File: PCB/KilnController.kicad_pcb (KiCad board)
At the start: 2 copper layers, 150 x 85 mm, 19 parts, among them J1 12V 3A PS Header, J2 Exhaust Fan Header, J3 Circulation Fan Header, J4 SD Card Module, J5 Exhaust Servo Header, J6 Intake Servo Header, Q1 FQP30N06L, Q2 FQP30N06L, U1 Raspberry Pi Pico 2W

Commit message: Current monitoring WIP
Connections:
- U1 pad 4: /SD_MISO -> /SD_SCK
- U1 pad 6: /SD_SCK -> /SD_MISO
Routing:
- net /+5V: track 147.0 -> 176.9 mm
- net /SD_SCK: track 10.2 -> 17.6 mm
- net /SD_MISO: track 10.2 -> 14.4 mm
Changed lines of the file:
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@@
 			)
 		)
-		(property "Datasheet" ""
+		(property "Datasheet" "~"
 			(at 0 0 0)
 			(layer "F.Fab")
@@
 			)
 		)
-		(property "Description" ""
+		(property "Description" "Generic screw terminal, single row, 01x04, script generated (kicad-library-utils/schlib/autogen/connector/)"
 			(at 0 0 0)
 			(layer "F.Fab")
@@
 			)
 		)
-		(property "Datasheet" ""
+		(property "Datasheet" "~"
 			(at 0 0 0)
 			(layer "F.Fab")
@@
 			)
 		)
-		(property "Description" ""
+		(property "Description" "Generic screw terminal, single row, 01x04, script generated (kicad-library-utils/schlib/autogen/connector/)"
 			(at 0 0 0)
 			(layer "F.Fab")
@@
 			)
 		)
-		(property "Datasheet" ""
+		(property "Datasheet" "~"
 			(at 0 0 0)
 			(layer "F.Fab")
@@
 			)
 		)
-		(property "Description" ""
+		(property "Description" "Generic screw terminal, single row, 01x04, script generated (kicad-library-utils/schlib/autogen/connector/)"
 			(at 0 0 0)
 			(layer "F.Fab")
@@
 			)
 		)
-		(property "Datasheet" ""
+		(property "Datasheet" "~"
 			(at 0 0 0)
 			(layer "F.Fab")
@@
 			)
 		)
-		(property "Description" ""
+		(property "Description" "Generic screw terminal, single row, 01x04, script generated (kicad-library-utils/schlib/autogen/connector/)"
 			(at 0 0 0)
 			(layer "F.Fab")
@@
 			)
 		)
-		(property "Datasheet" ""
+		(property "Datasheet" "https://datasheets.raspberrypi.com/picow/pico-2-w-datasheet.pdf"
 			(at 8.89 24.13 90)
 			(layer "F.Fab")
@@
 			(layers "*.Cu" "*.Mask")
 			(remove_unused_layers no)
-			(net 12 "/SD_MISO")
+			(net 10 "/SD_SCK")
 			(pinfunction "GP2")
 			(pintype "bidirectional")
@@
 			(layers "*.Cu" "*.Mask")
 			(remove_unused_layers no)
-			(net 10 "/SD_SCK")
+			(net 12 "/SD_MISO")
 			(pinfunction "GP4")
 			(pintype "bidirectional")
@@
 	)
 	(segment
+		(start 142 119)
+		(end 147 124)
+		(width 0.25)
+		(layer "F.Cu")
+		(net 2)
+	)
+	(segment
 		(start 89.36 88.22)
 		(end 86.82 88.22)
@@
 	)
 	(segment
-		(start 154.08 140)
-		(end 157.08 137)
+		(start 98.68 119)
+		(end 142 119)
 		(width 0.25)
 		(layer "F.Cu")
@@
 	)
 	(segment
-		(start 98.68 119)
-		(end 94.68 115)
+		(start 147 124)
+		(end 147 140)
+		(width 0.25)
+		(layer "F.Cu")
+		(net 2)
+	)
+	(segment
+		(start 154.08 140)
+		(end 157.08 137)
 		(width 0.25)
 		(layer "F.Cu")
@@
 	(segment
 		(start 145 140)
-		(end 154.08 140)
+		(end 147 140)
 		(width 0.25)
 		(layer "F.Cu")
@@
 	)
 	(segment
-		(start 131 119)
+		(start 94.68 115)
 		(end 98.68 119)
 		(width 0.25)
@@
 	)
 	(segment
-		(start 134 122)
-		(end 131 119)
-		(width 0.25)
-		(layer "F.Cu")
-		(net 2)
-	)
-	(segment
 		(start 83 111)
 		(end 83 92.04)
@@
 	)
 	(segment
+		(start 147 140)
+		(end 154.08 140)
+		(width 0.25)
+		(layer "F.Cu")
+		(net 2)
+	)
+	(segment
 		(start 94.68 115)
 		(end 90.68 111)
@@
 	)
 	(segment
-		(start 99.52 112.22)
+		(start 94.44 106)
+		(end 96.015 104.425)
+		(width 0.25)
+		(layer "F.Cu")
+		(net 10)
+	)
+	(segment
+		(start 99.825991 104.425)
+		(end 100.935 105.534009)
+		(width 0.25)
+		(layer "F.Cu")
+		(net 10)
+	)
+	(segment
+		(start 96.015 104.425)
+		(end 99.825991 104.425)
+		(width 0.25)
+		(layer "F.Cu")
+		(net 10)
+	)
+	(segment
+		(start 100.935 113.635)
 		(end 102.3 115)
 		(width 0.25)
@@
 	)
 	(segment
-		(start 99.52 106)
-		(end 99.52 112.22)
+		(start 100.935 105.534009)
+		(end 100.935 113.635)
 		(width 0.25)
 		(layer "F.Cu")
@@
 	)
 	(segment
-		(start 94.44 106)
-		(end 94.44 112.22)
+		(start 99.52 106)
+		(end 98.395 104.875)
+		(width 0.25)
+		(layer "F.Cu")
+		(net 12)
+	)
+	(segment
+		(start 95.855 105.534009)
+		(end 95.855 113.635)
 		(width 0.25)
 		(layer "F.Cu")
@@
 	)
 	(segment
-		(start 94.44 112.22)
+		(start 95.855 113.635)
 		(end 97.22 115)
 		(width 0.25)
 		(layer "F.Cu")
+		(net 12)
+	)
+	(segment
+		(start 98.395 104.875)
+		(end 96.514009 104.875)
+		(width 0.25)
+		(layer "F.Cu")
+		(net 12)
+	)
+	(segment
+		(start 96.514009 104.875)
+		(end 95.855 105.534009)
+		(width 0.25)
+		(layer "F.Cu")

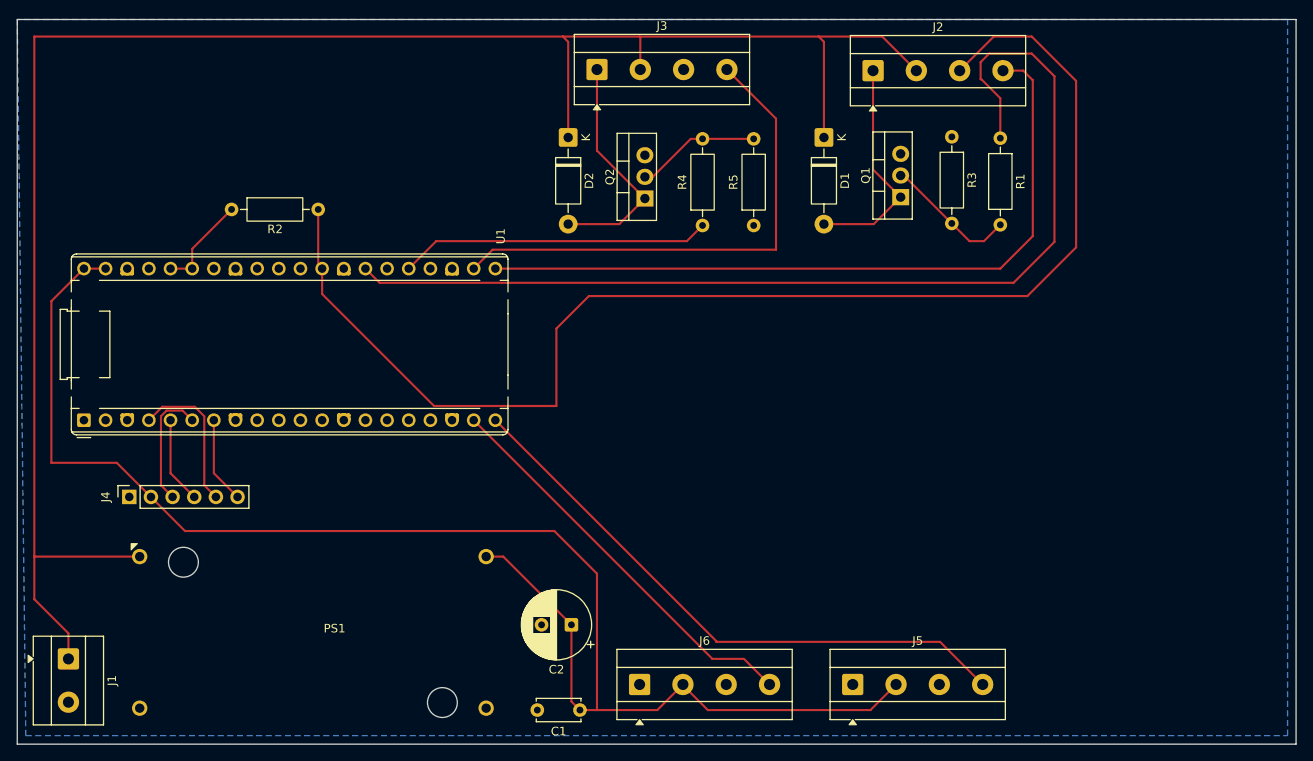
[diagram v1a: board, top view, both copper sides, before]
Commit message: Working current monitors, with updated layout
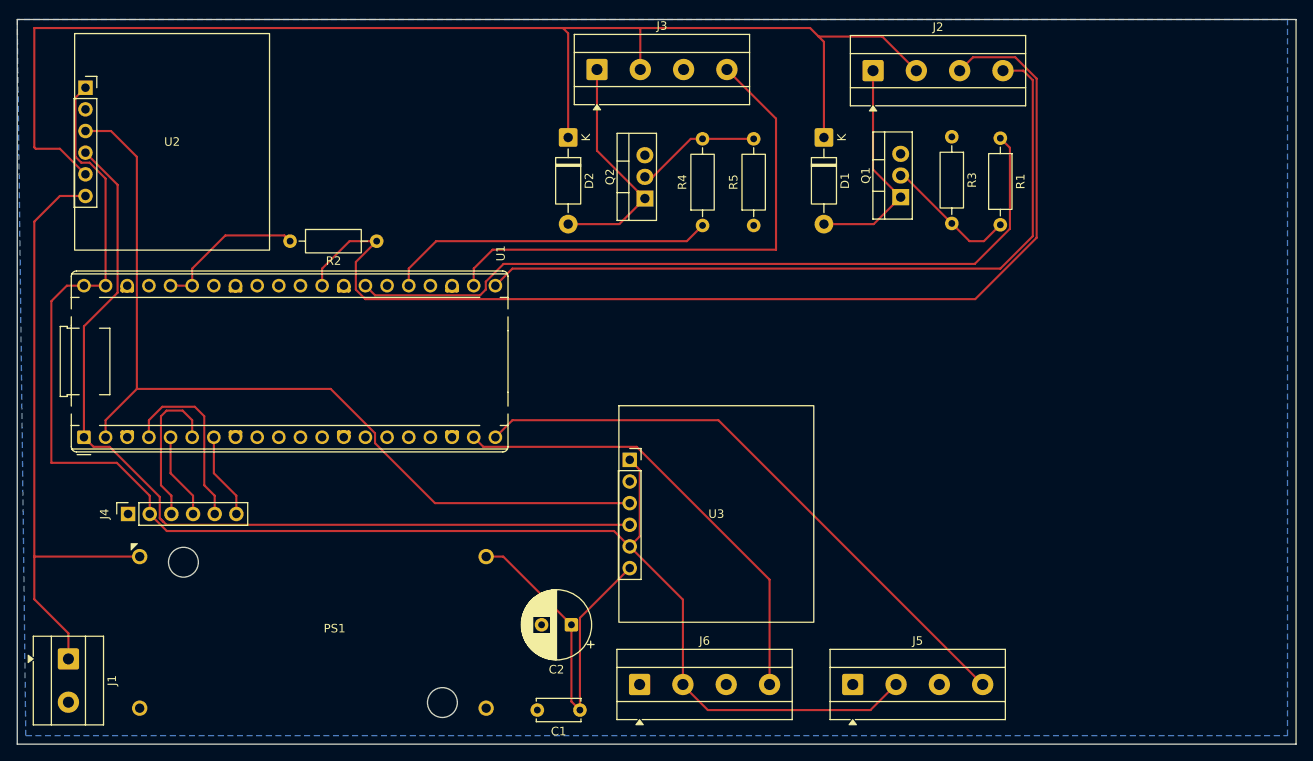
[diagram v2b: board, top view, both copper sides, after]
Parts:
- added U2: INA219 Current Sensor (12V), KilnFootprintLibrary:INA219_Module, F.Cu at (87.0, 67.0)
- added U3: INA219 Current Sensor (5V), KilnFootprintLibrary:INA219_Module, F.Cu at (150.8, 110.7)
- moved R2 7.80 mm to (111.0, 85.0)
- moved J4 2.00 mm to (92.0, 117.0)
- moved U1 2.00 mm to (86.8, 108.0)
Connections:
- C1 pad 1: /+5V -> /+5V_SRC
- C2 pad 1: /+5V -> /+5V_SRC
- J1 pad 1: /+12V -> /+12V_SRC
- PS1 pad 1: /+12V -> /+12V_SRC
- PS1 pad 3: /+5V -> /+5V_SRC
- U1 pad 1: unconnected-(U1-GP0-Pad1) -> /I2C0_SDA
- U1 pad 2: unconnected-(U1-GP1-Pad2) -> /I2C0_SCL
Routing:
- net /I2C0_SDA: track 0.00 -> 106.9 mm
- net /I2C0_SCL: track 0.00 -> 105.7 mm
- net /+12V_SRC: track 0.00 -> 72.6 mm
- net /+12V: track 220.2 -> 156.9 mm
- net /+5V_SRC: track 0.00 -> 42.8 mm
- net /FAN_EX_GATE: track 123.0 -> 90.9 mm
- net /FAN_EX_TACH: track 154.0 -> 129.1 mm
- net /+3V3: track 11.4 -> 17.9 mm
- net /SERVO_INTAKE: track 47.5 -> 53.9 mm
- net /+5V: track 176.9 -> 182.5 mm
- net /SD_SCK: track 17.6 -> 21.6 mm
- net /SD_MISO: track 14.4 -> 18.4 mm
- net /FAN_CIR_PWM: track 59.9 -> 61.9 mm
- net /FAN_CIR_GATE: track 36.6 -> 38.6 mm
- net /FAN_EX_PWM: track 86.9 -> 87.7 mm
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
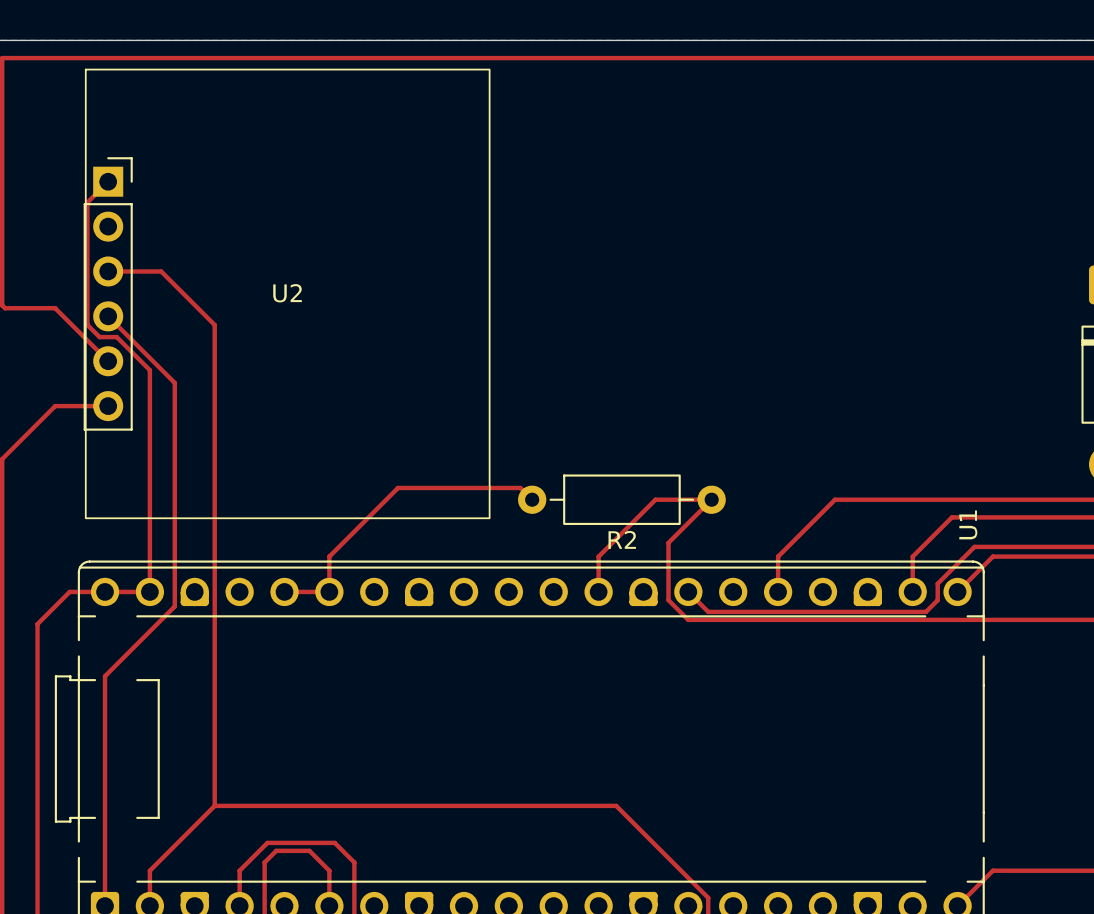
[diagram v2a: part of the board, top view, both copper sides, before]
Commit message: Controller and KiCad for SHT31D sensors
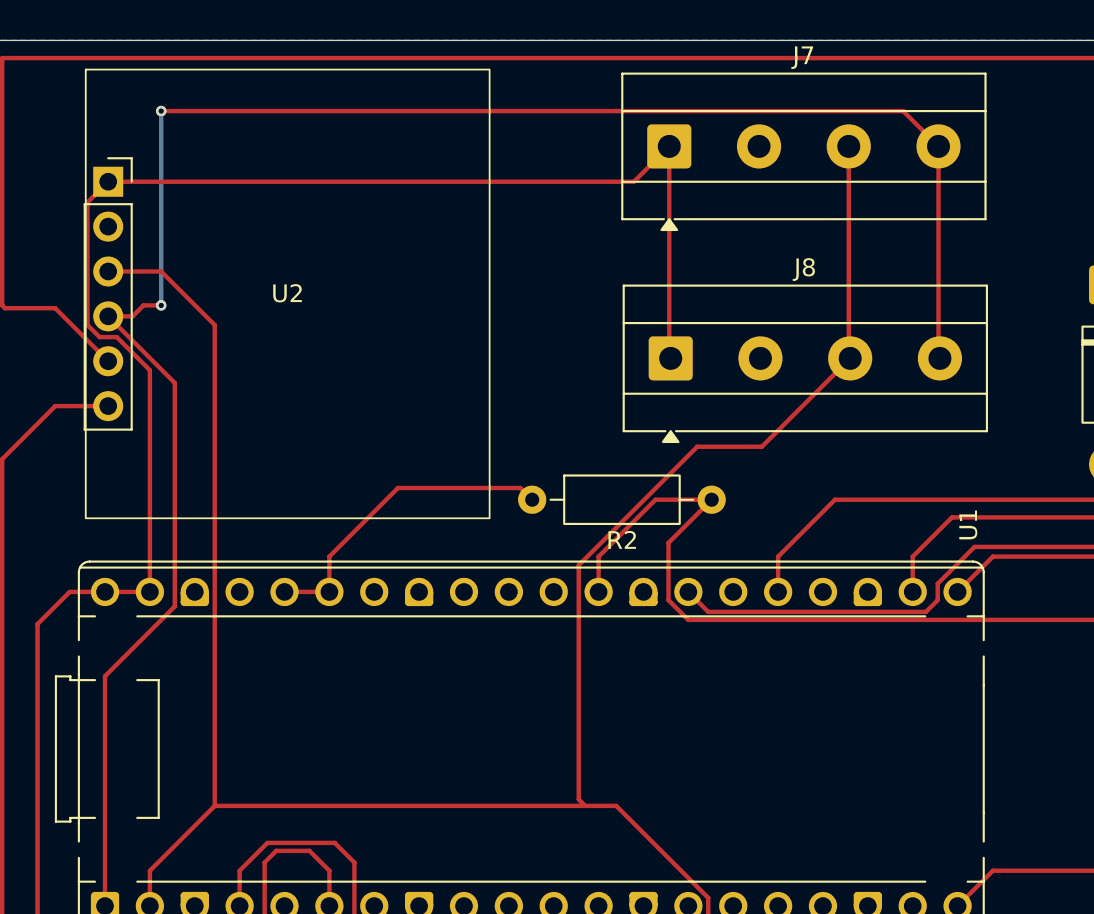
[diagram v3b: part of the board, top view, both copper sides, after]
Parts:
- added J7: Lumber Zone SHT31 Header, KilnFootprintLibrary:TerminalBlock_MetzConnect_Type101_RT01604HBWC_1x04_P5.08mm_Horizontal, F.Cu at (118.8, 65.0)
- added J8: Intake Zone SHT31 Header, KilnFootprintLibrary:TerminalBlock_MetzConnect_Type101_RT01604HBWC_1x04_P5.08mm_Horizontal, F.Cu at (118.8, 77.0)
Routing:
- net /I2C0_SDA: track 106.9 -> 178.0 mm, vias 0 -> 2
- net /I2C0_SCL: track 105.7 -> 151.8 mm
- net /+5V: track 182.5 -> 227.1 mm

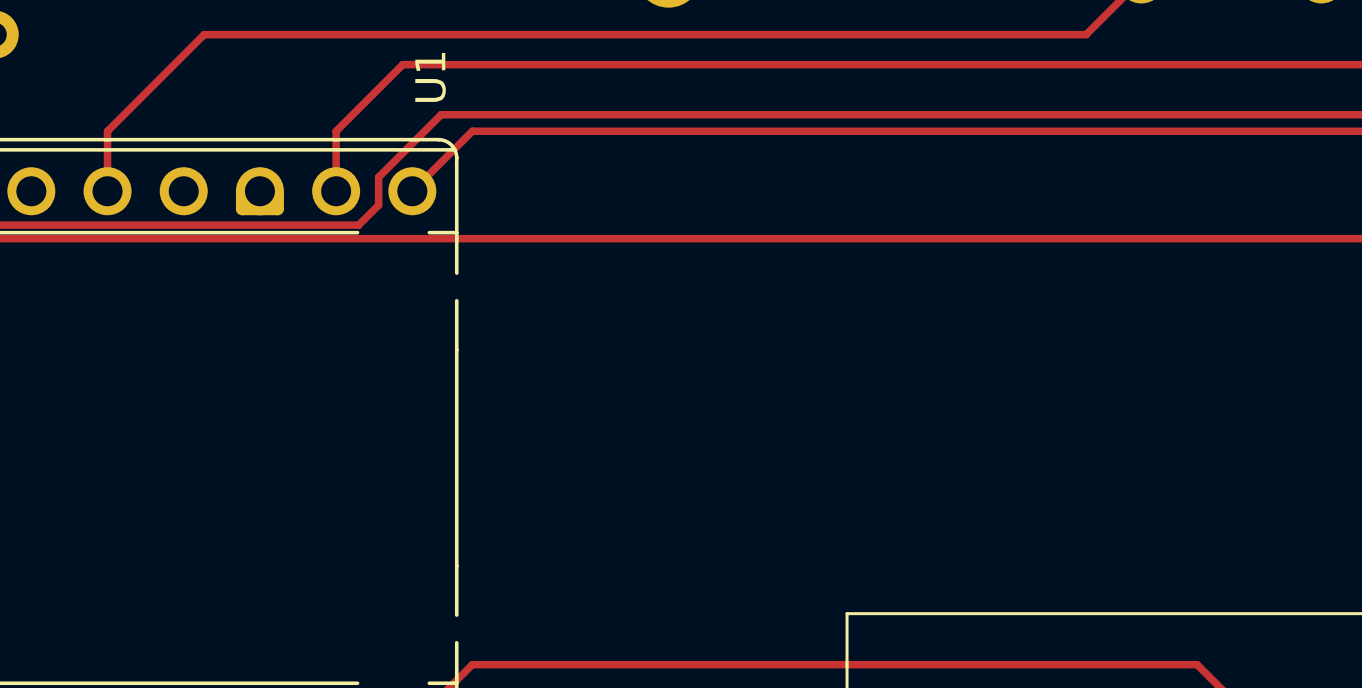
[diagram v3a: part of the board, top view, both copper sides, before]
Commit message: Heater SSR controller and PCB update
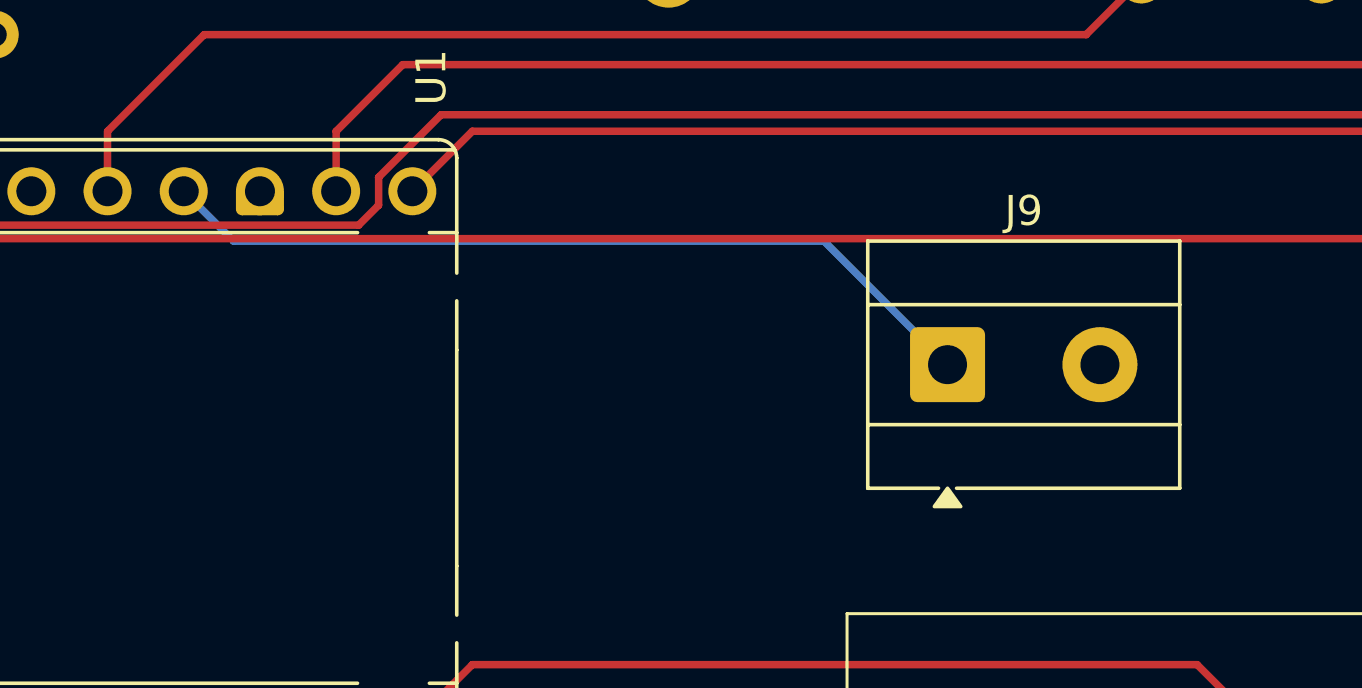
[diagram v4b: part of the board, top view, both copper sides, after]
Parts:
- added J9: Heater SSR Header, TerminalBlock_MetzConnect:TerminalBlock_MetzConnect_Type101_RT01602HBWC_1x02_P5.08mm_Horizontal, F.Cu at (152.9, 96.0)
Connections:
- U1 pad 24: unconnected-(U1-GP18-Pad24) -> /HEATER_SSR
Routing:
- net /HEATER_SSR: track 0.00 -> 27.9 mm

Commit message: Working display driver with schematic and layout
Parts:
- added J10: Display Header, KilnFootprintLibrary:TerminalBlock_MetzConnect_Type101_RT01604HBWC_1x04_P5.08mm_Horizontal, F.Cu at (163.4, 137.0)
- added J11: Display Button Header, TerminalBlock_MetzConnect:TerminalBlock_MetzConnect_Type101_RT01602HBWC_1x02_P5.08mm_Horizontal, F.Cu at (150.5, 136.9)
- moved J6 34.0 mm to (186.0, 137.0)
- moved J5 32.0 mm to (209.0, 137.0)
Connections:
- U1 pad 11: unconnected-(U1-GP8-Pad11) -> /DISPLAY_TX
- U1 pad 12: unconnected-(U1-GP9-Pad12) -> /DISPLAY_RX
- U1 pad 14: unconnected-(U1-GP10-Pad14) -> /DISPLAY_BUTTON
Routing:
- net /DISPLAY_TX: track 0.00 -> 90.1 mm, vias 0 -> 1
- net /DISPLAY_RX: track 0.00 -> 81.2 mm, vias 0 -> 1
- net /DISPLAY_BUTTON: track 0.00 -> 54.8 mm, vias 0 -> 1
- net /+5V: track 227.1 -> 263.4 mm
- net /SERVO_EXHAUST: track 70.8 -> 104.0 mm
- net /SERVO_INTAKE: track 53.9 -> 84.5 mm
- net /I2C0_SCL: track 151.8 -> 165.2 mm
- net /I2C0_SDA: vias 2 -> 1

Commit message: Update Display Button GPIO
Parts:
- added J12: Moisture Probe 1 Header, TerminalBlock_MetzConnect:TerminalBlock_MetzConnect_Type101_RT01602HBWC_1x02_P5.08mm_Horizontal, F.Cu at (166.5, 95.9)
- added J13: Moisture Probe 2 Header, TerminalBlock_MetzConnect:TerminalBlock_MetzConnect_Type101_RT01602HBWC_1x02_P5.08mm_Horizontal, F.Cu at (179.5, 95.9)
- added R6: 100k, Resistor_THT:R_Axial_DIN0207_L6.3mm_D2.5mm_P10.16mm_Horizontal, F.Cu at (113.9, 114.0)
- added R7: 100k, Resistor_THT:R_Axial_DIN0207_L6.3mm_D2.5mm_P10.16mm_Horizontal, F.Cu at (127.9, 114.0)
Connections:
- U1 pad 10: unconnected-(U1-GP7-Pad10) -> /PROBE_2_DRIVER
- U1 pad 14: /DISPLAY_BUTTON -> /LORA_SCK
- U1 pad 15: unconnected-(U1-GP11-Pad15) -> /LORA_TX
- U1 pad 16: unconnected-(U1-GP12-Pad16) -> /LORA_RX
- U1 pad 17: unconnected-(U1-GP13-Pad17) -> /LORA_CS
- U1 pad 26: unconnected-(U1-GP20-Pad26) -> /DISPLAY_BUTTON
- U1 pad 31: unconnected-(U1-GP26_A0-Pad31) -> /PROBE_1_ADC
- U1 pad 32: unconnected-(U1-GP27_A1-Pad32) -> /PROBE_2_ADC
- U1 pad 34: unconnected-(U1-GP28_A2-Pad34) -> /LORA_RST
- U1 pad 9: unconnected-(U1-GP6-Pad9) -> /PROBE_1_DRIVER
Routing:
- net /PROBE_2_ADC: track 0.00 -> 96.9 mm
- net /PROBE_1_ADC: track 0.00 -> 76.6 mm, vias 0 -> 1
- net /DISPLAY_BUTTON: track 54.8 -> 76.1 mm
- net /PROBE_2_DRIVER: track 0.00 -> 20.7 mm
- net /PROBE_1_DRIVER: track 0.00 -> 9.27 mm
- net /DISPLAY_RX: track 81.2 -> 82.9 mm
